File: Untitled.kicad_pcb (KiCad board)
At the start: 2 copper layers, 37 x 37 mm, 20 parts, among them J1 Battery Connector, J2 Pyro Ignition Terminal, J3 Pyro Voltage Terminal, Q1 Q_NMOS_DGS, Q2 Q_NMOS_DGS, Q3 Q_NMOS_DGS, U1 XIAO-ESP32-S3-SMD, U3 LSM6DSO32, U4 Barometer

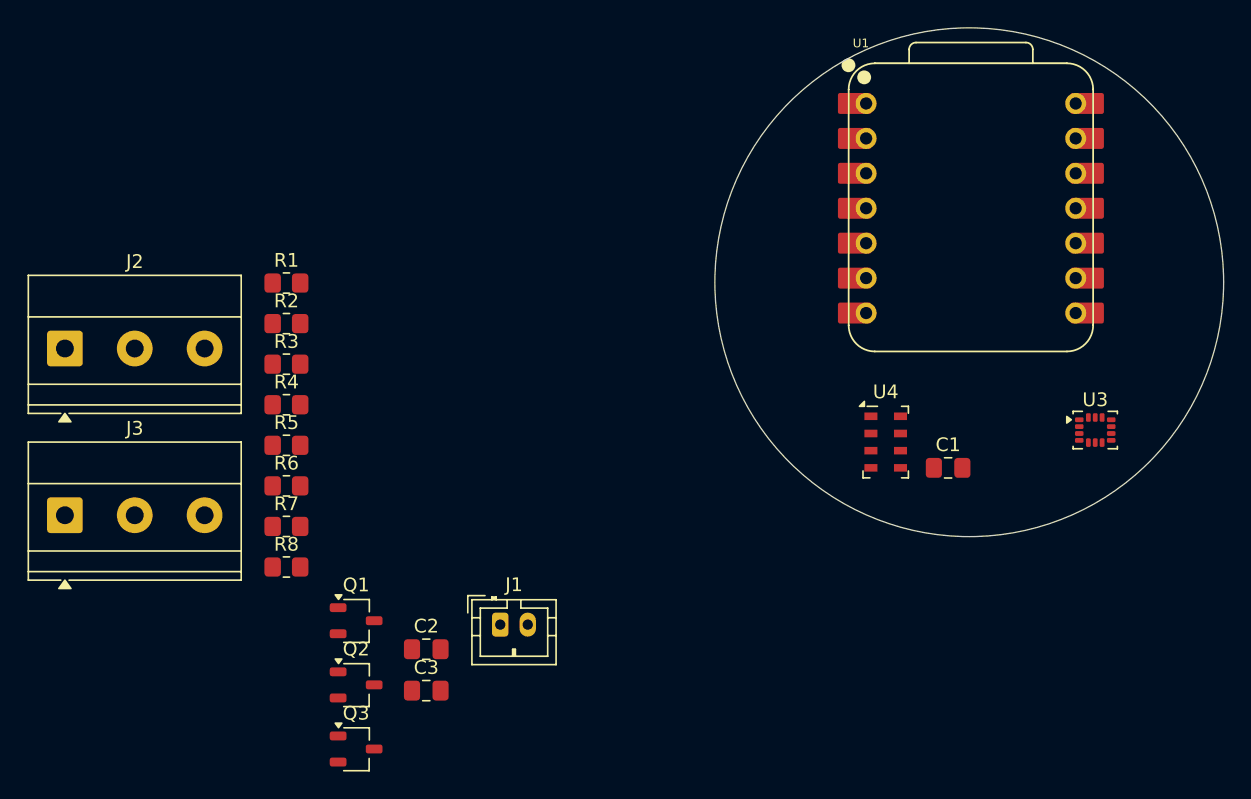
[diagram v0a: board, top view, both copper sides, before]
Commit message: Experimental Layout
Changed screw terminal footprint to accurately reflect existing club stock of smaller terminals (2.54mm pitch thru-hole). Experimented with trying to make a single board layout work for the flight computer.
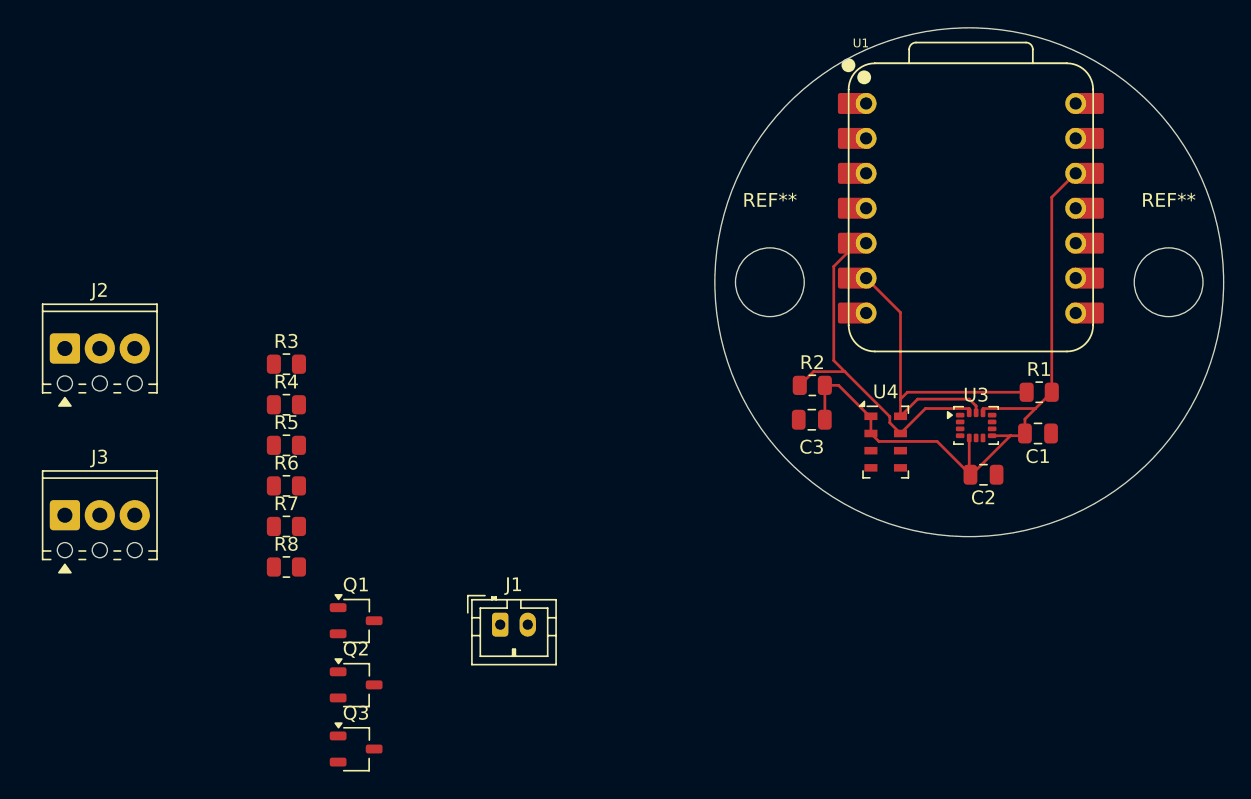
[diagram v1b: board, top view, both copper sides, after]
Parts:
- added REF**: MountingHole_5mm, MountingHole:MountingHole_5mm, F.Cu at (220.5, 67.5)
- added REF**: MountingHole_5mm, MountingHole:MountingHole_5mm, F.Cu at (191.5, 67.5)
- C1, C2, C3: footprint Capacitor_SMD:C_0805_2012Metric_Pad1.18x1.45mm_HandSolder -> Capacitor_SMD:C_0805_2012Metric
- J2, J3: footprint TerminalBlock_Phoenix:TerminalBlock_Phoenix_MKDS-1,5-3-5.08_1x03_P5.08mm_Horizontal -> TerminalBlock_Phoenix:TerminalBlock_Phoenix_MPT-0,5-3-2.54_1x03_P2.54mm_Horizontal
- R1, R2, R3, R4, R5, R6, R7, R8: footprint Resistor_SMD:R_0805_2012Metric_Pad1.20x1.40mm_HandSolder -> Resistor_SMD:R_0805_2012Metric
- U4: value Barometer -> MS5611-01BA
- moved R1 55.3 mm to (211.1, 75.5)
- moved C2 42.5 mm to (207.0, 81.5), turned to 180 degrees
- moved R2 38.5 mm to (194.6, 75.0)
- moved C3 34.3 mm to (194.6, 77.5)
- moved U3 8.67 mm to (206.5, 77.9)
- moved C1 7.00 mm to (211.0, 78.5), turned to 180 degrees
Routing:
- net +3.3V: track 0.00 -> 50.7 mm
- net /SCL: track 0.00 -> 27.2 mm
- net /SDA: track 0.00 -> 27.0 mm

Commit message: Basic Schematic (NO PCB DESIGN DONE)
Removed any PCB design so people can fork off and do their own PCB designs.
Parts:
- J2: value Pyro Ignition Terminal -> Top Screw Terminal; footprint TerminalBlock_Phoenix:TerminalBlock_Phoenix_MPT-0,5-3-2.54_1x03_P2.54mm_Horizontal -> TerminalBlock_Phoenix:TerminalBlock_Phoenix_MPT-0,5-4-2.54_1x04_P2.54mm_Horizontal
- J3: value Pyro Voltage Terminal -> Bottom Screw Terminal; footprint TerminalBlock_Phoenix:TerminalBlock_Phoenix_MPT-0,5-3-2.54_1x03_P2.54mm_Horizontal -> TerminalBlock_Phoenix:TerminalBlock_Phoenix_MPT-0,5-2-2.54_1x02_P2.54mm_Horizontal
- moved R1 33.1 mm to (178.1, 72.5)
- moved C1 33.0 mm to (178.1, 76.5)
- moved R2 24.2 mm to (170.9, 80.0)
- moved C2 23.8 mm to (183.4, 84.5)
- moved U3 23.2 mm to (183.5, 81.1)
- moved U4 21.0 mm to (183.1, 91.6)
- moved C3 20.1 mm to (175.9, 85.0)
- moved J3 5.42 mm to (142.5, 79.5)
- moved J2 3.63 mm to (142.5, 69.5)
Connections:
- J2 pad 1: /APPO -> +3.3V
- J2 pad 2: /MAIN -> /APPO
- J2 pad 3: /MOTOR -> +3.3V
- J3 pad 1: +BATT -> +3.3V
- J3 pad 2: +BATT -> /MOTOR
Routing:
- net +3.3V: track 50.7 -> 0.00 mm
- net /SCL: track 27.2 -> 0.00 mm
- net /SDA: track 27.0 -> 0.00 mm

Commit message: cdr ready pcb design
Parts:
- C1, C2: footprint Capacitor_SMD:C_0805_2012Metric -> Capacitor_SMD:C_0603_1608Metric
- C3: footprint Capacitor_SMD:C_0805_2012Metric -> Capacitor_SMD:C_0603_1608Metric; moved to B.Cu
- J1, J3, Q3, U4: moved to B.Cu
- R1, R2, R3, R4, R5, R6: footprint Resistor_SMD:R_0805_2012Metric -> Resistor_SMD:R_0402_1005Metric
- R7, R8: footprint Resistor_SMD:R_0805_2012Metric -> Resistor_SMD:R_0402_1005Metric; moved to B.Cu
- moved J2 68.1 mm to (210.2, 76.4)
- moved J1 56.8 mm to (218.5, 60.0), turned to 90 degrees
- moved R5 54.7 mm to (211.0, 81.5)
- moved R6 54.7 mm to (211.0, 84.5)
- moved J3 54.7 mm to (197.0, 76.5), turned to 180 degrees
- moved R4 49.2 mm to (205.5, 74.0), turned to -90 degrees
- moved Q3 49.2 mm to (207.0, 83.0), turned to -90 degrees
- moved Q2 47.6 mm to (207.0, 83.0), turned to -90 degrees
- moved R7 46.5 mm to (202.7, 81.5), turned to 180 degrees
- moved R8 46.5 mm to (202.7, 84.5), turned to 180 degrees
- moved R3 46.5 mm to (202.5, 79.0)
- moved Q1 44.3 mm to (202.5, 75.5), turned to -90 degrees
- moved R2 30.3 mm to (194.5, 61.0)
- moved C1 27.9 mm to (205.8, 79.5)
- moved U4 26.2 mm to (204.7, 76.9)
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- renumbered REF** to trust, REF** to trustme
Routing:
- net +3.3V: track 0.00 -> 85.5 mm, vias 0 -> 1
- net -BATT: track 0.00 -> 81.6 mm, vias 0 -> 3
- net /CONT 2: track 0.00 -> 47.9 mm, vias 0 -> 3
- net /CONT 3: track 0.00 -> 37.9 mm
- net /SCL: track 0.00 -> 37.6 mm, vias 0 -> 1
- net /SDA: track 0.00 -> 37.3 mm, vias 0 -> 1
- net /IGNIT 2: track 0.00 -> 31.9 mm, vias 0 -> 1
- net /CONT 1: track 0.00 -> 27.6 mm
- net /IGNIT 3: track 0.00 -> 24.3 mm
- net /MOTOR: track 0.00 -> 21.4 mm
- net /IGNIT 1: track 0.00 -> 17.0 mm
- net /MAIN: track 0.00 -> 12.8 mm
- net /APPO: track 0.00 -> 10.2 mm
- net +BATT: track 0.00 -> 8.31 mm
